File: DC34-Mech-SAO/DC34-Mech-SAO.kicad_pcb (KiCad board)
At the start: 2 copper layers, 27.9 x 38 mm, 20 parts, among them J1 Conn_01x06_Male, J2 Conn_01x03_Male, U1 ATtiny816-M

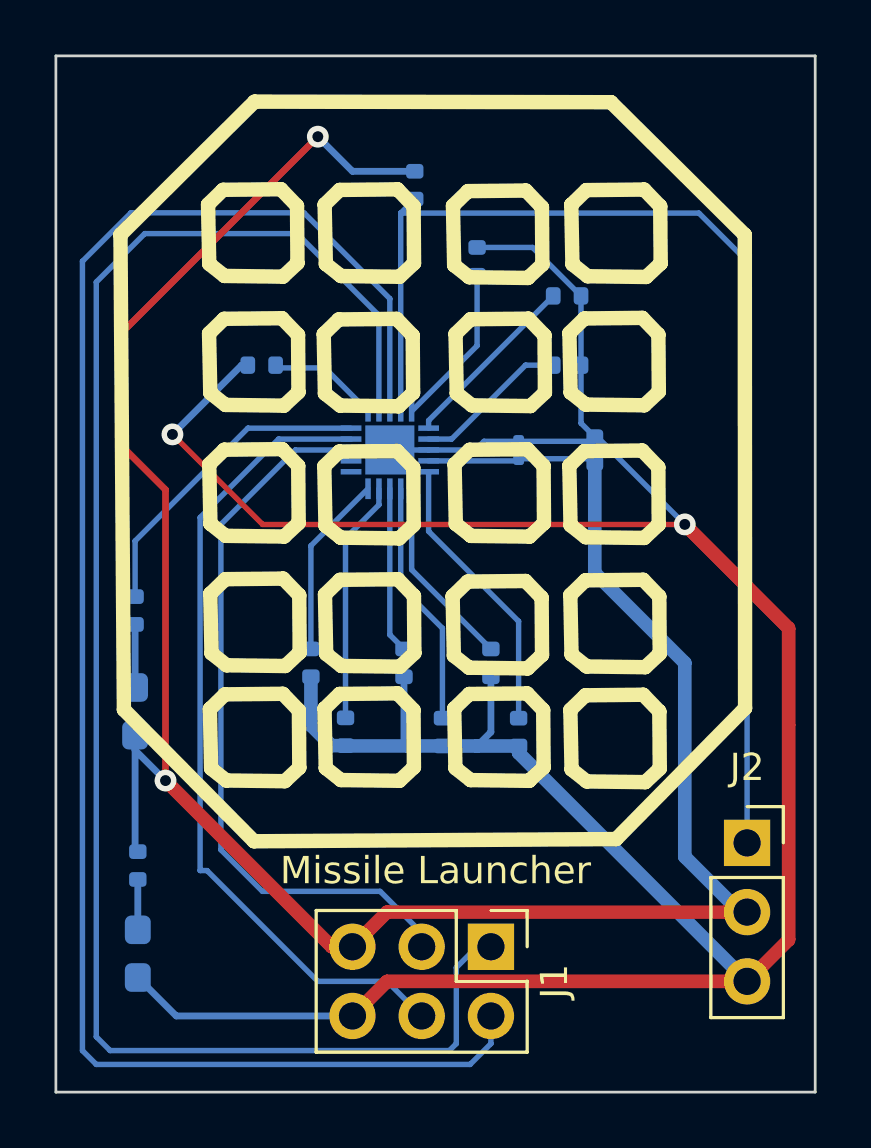
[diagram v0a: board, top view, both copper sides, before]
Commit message: change_3
added laser cannon
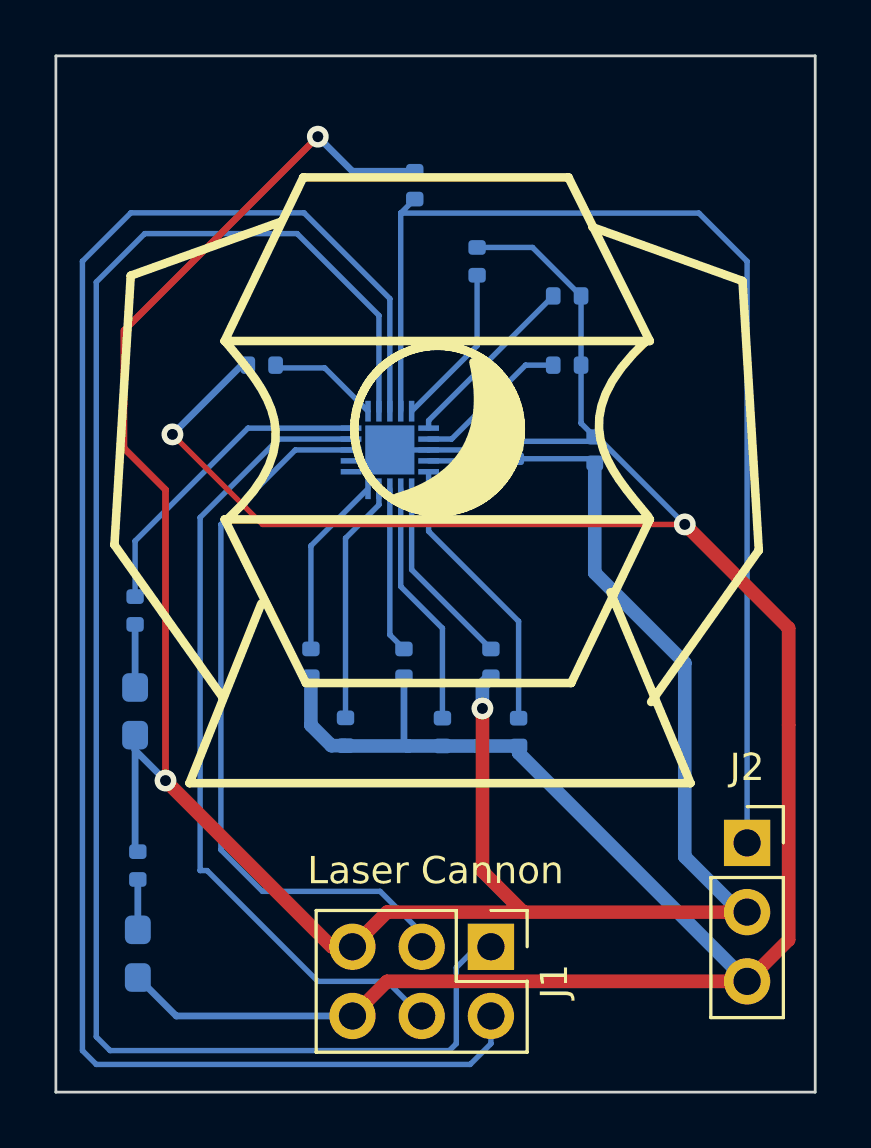
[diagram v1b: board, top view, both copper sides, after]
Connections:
- R5 pad 2: GND -> PWR
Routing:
- net PWR: track 87.2 -> 96.6 mm, vias 1 -> 2
- net GND: track 115.9 -> 113.1 mm
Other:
- board text added: "Laser Cannon"
- board text removed: "Missile Launcher"

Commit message: Added silkscreen
Added descriptive text to board.
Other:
- board text added: "Designed by CPEC in Arizona Manufactured in China"
- board text added: "GND"
- board text added: "Mech Fighters SAO Rev 1"
- board text added: "PWR"
- board text added: "UPDI"
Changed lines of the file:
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@@
 		(layer "Edge.Cuts")
+	)
+	(gr_text "UPDI"
+		(at 153.5 90 270)
+		(layer "F.SilkS")
+		(effects
+			(font
+				(size 0.5 0.5)
+				(thickness 0.07)
+			)
+			(justify left bottom)
+		)
+	)
+	(gr_text "PWR"
+		(at 153.5 92.5 270)
+		(layer "F.SilkS")
+		(effects
+			(font
+				(size 0.5 0.5)
+				(thickness 0.07)
+			)
+			(justify left bottom)
+		)
+	)
+	(gr_text "GND"
+		(at 153.5 95.5 270)
+		(layer "F.SilkS")
+		(effects
+			(font
+				(size 0.5 0.5)
+				(thickness 0.07)
+			)
+			(justify left bottom)
+		)
 	)
 	(gr_text "Laser Cannon"
@@
 		)
 	)
+	(gr_text "Mech Fighters SAO Rev 1"
+		(at 153.5 81 0)
+		(layer "B.SilkS")
+		(effects
+			(font
+				(size 1 1)
+				(thickness 0.15)
+			)
+			(justify left bottom mirror)
+		)
+	)
+	(gr_text "Designed by CPEC in Arizona\nManufactured in China"
+		(at 143 92 0)
+		(layer "B.SilkS")
+		(effects
+			(font
+				(size 1 1)
+				(thickness 0.15)
+			)
+			(justify bottom mirror)
+		)
+	)
